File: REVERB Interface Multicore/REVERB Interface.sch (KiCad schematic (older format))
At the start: 59 parts, among them J1 RPiZeroW, J2 Iridium, J3 APRS, J4 Antenna, J5 UPDI, M1 MountingHole_Pad, M2 MountingHole_Pad, M3 MountingHole_Pad, M4 MountingHole_Pad, M5 PiMount, M6 PiMount, M7 PiMount, M8 PiMount, U1 LSM9DS1BOB, U2 MAX3232, U3 ATtiny1604-SS, U4 TXB0104D

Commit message: tie OE high
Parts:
- removed R13: 10K, Resistor_SMD:R_0805_2012Metric_Pad1.20x1.40mm_HandSolder, symbol Device:R
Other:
- moved on the sheet: J2, J3, J4, JP1, JP2, JP3, JP4

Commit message: Add decoupling
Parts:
- added C12: 22uF, Capacitor_Tantalum_SMD:CP_EIA-6032-28_Kemet-C_Pad2.25x2.35mm_HandSolder, symbol Device:CP
- added C13, C17, C18, C20, C8: 100uF, Capacitor_Tantalum_SMD:CP_EIA-7343-43_Kemet-X_Pad2.25x2.55mm_HandSolder, symbol Device:CP
- added C14, C15, C16, C19, C21, C22, C23, C9: 47uF, Capacitor_Tantalum_SMD:CP_EIA-6032-28_Kemet-C_Pad2.25x2.35mm_HandSolder, symbol Device:CP
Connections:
- wire segments 95 -> 107

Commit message: fix imu implementation on multicore branch
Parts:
- removed U1: LSM9DS1BOB, REVERB Interface:LSM9DS1BOB, symbol REVERBSym:LSM9DS1BOB
- added U1: IMU, REVERB Interface:LSM9DS1-BNO055, symbol REVERBSym:IMU
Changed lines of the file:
@@
 Wire Notes Line
 	6900 6700 6900 3650
-$Comp
-L REVERBSym:LSM9DS1BOB U1
-U 1 1 617E2B02
-P 10200 4650
-F 0 "U1" H 10678 4696 50  0000 L CNN
-F 1 "LSM9DS1BOB" H 10678 4605 50  0000 L CNN
-F 2 "REVERB Interface:LSM9DS1BOB" H 10200 4650 50  0001 C CNN
-F 3 "" H 10200 4650 50  0001 C CNN
-	1    10200 4650
-	1    0    0    -1
-$EndComp
-Text Label 9900 5050 3    50   ~ 0
+Text Label 9800 5050 3    50   ~ 0
 SW9
 Wire Wire Line
@@
 	1    0    0    -1
 $EndComp
+$Comp
+L REVERBSym:IMU U1
+U 1 1 618A2546
+P 10200 4650
+F 0 "U1" H 10678 4563 50  0000 L CNN
+F 1 "IMU" H 10678 4472 50  0000 L CNN
+F 2 "REVERB Interface:LSM9DS1-BNO055" H 10200 4650 50  0001 C CNN
+F 3 "" H 10200 4650 50  0001 C CNN
+	1    10200 4650
+	1    0    0    -1
+$EndComp

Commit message: intermediate commit
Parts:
- U1: footprint REVERB Interface:LSM9DS1-BNO055 -> REVERB Interface:BNO055
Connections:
- net EPSSCL: now also U1.5 (SCL)
- net EPSSDA: now also U1.4 (SDA)
- net GND: now also U1.3 (GND)
- net SW9: now also U1.1 (VIN)
- net IMURST: now reaches J1.32 (12(PWM0))
- net IMURST: now also U1.6 (RST)
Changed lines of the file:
@@
 Wire Notes Line
 	6900 6700 6900 3650
-Text Label 9800 5050 3    50   ~ 0
+Text Label 9950 5050 3    50   ~ 0
 SW9
 Wire Wire Line
-	10000 5050 10000 5250
+	10150 5050 10150 5250
 $Comp
 L power:GND #PWR0129
 U 1 1 617E7DA1
-P 10000 5250
-F 0 "#PWR0129" H 10000 5000 50  0001 C CNN
-F 1 "GND" H 10005 5077 50  0000 C CNN
-F 2 "" H 10000 5250 50  0001 C CNN
-F 3 "" H 10000 5250 50  0001 C CNN
-	1    10000 5250
-	1    0    0    -1
-$EndComp
-Text Label 10100 5050 3    50   ~ 0
+P 10150 5250
+F 0 "#PWR0129" H 10150 5000 50  0001 C CNN
+F 1 "GND" H 10155 5077 50  0000 C CNN
+F 2 "" H 10150 5250 50  0001 C CNN
+F 3 "" H 10150 5250 50  0001 C CNN
+	1    10150 5250
+	1    0    0    -1
+$EndComp
+Text Label 10350 5050 3    50   ~ 0
 EPSSCL
-Text Label 10200 5050 3    50   ~ 0
+Text Label 10250 5050 3    50   ~ 0
 EPSSDA
 Text Notes 9700 4200 0    50   ~ 0
@@
 F 0 "U1" H 10678 4563 50  0000 L CNN
 F 1 "IMU" H 10678 4472 50  0000 L CNN
-F 2 "REVERB Interface:LSM9DS1-BNO055" H 10200 4650 50  0001 C CNN
+F 2 "REVERB Interface:BNO055" H 10200 4650 50  0001 C CNN
 F 3 "" H 10200 4650 50  0001 C CNN
 	1    10200 4650
 	1    0    0    -1
 $EndComp
+Text Label 10450 5050 3    50   ~ 0
+IMURST
+Text Label 4600 1200 2    50   ~ 0
+IMURST
 $EndSCHEMATC

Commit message: RI line
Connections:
- net GND: now also J2.15 (Pin_15)
- net RI: now reaches J1.12 (18(PWM0))
- net RI: now also J2.8 (Pin_8)
- no-connect marks 99 -> 97
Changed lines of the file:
@@
 NoConn ~ 8800 4700
 NoConn ~ 8800 4800
-NoConn ~ 8800 4900
 NoConn ~ 8800 5000
 NoConn ~ 8800 5100
 NoConn ~ 8800 5200
-NoConn ~ 9300 4500
 NoConn ~ 9300 4800
 NoConn ~ 9300 4900
@@
 Text Label 4600 1200 2    50   ~ 0
 IMURST
+Wire Wire Line
+	9550 5000 9550 4500
+Wire Wire Line
+	9550 4500 9300 4500
+Connection ~ 9550 5000
+Text Label 8800 4900 2    50   ~ 0
+RI
+Text Label 4600 2200 2    50   ~ 0
+RI
 $EndSCHEMATC

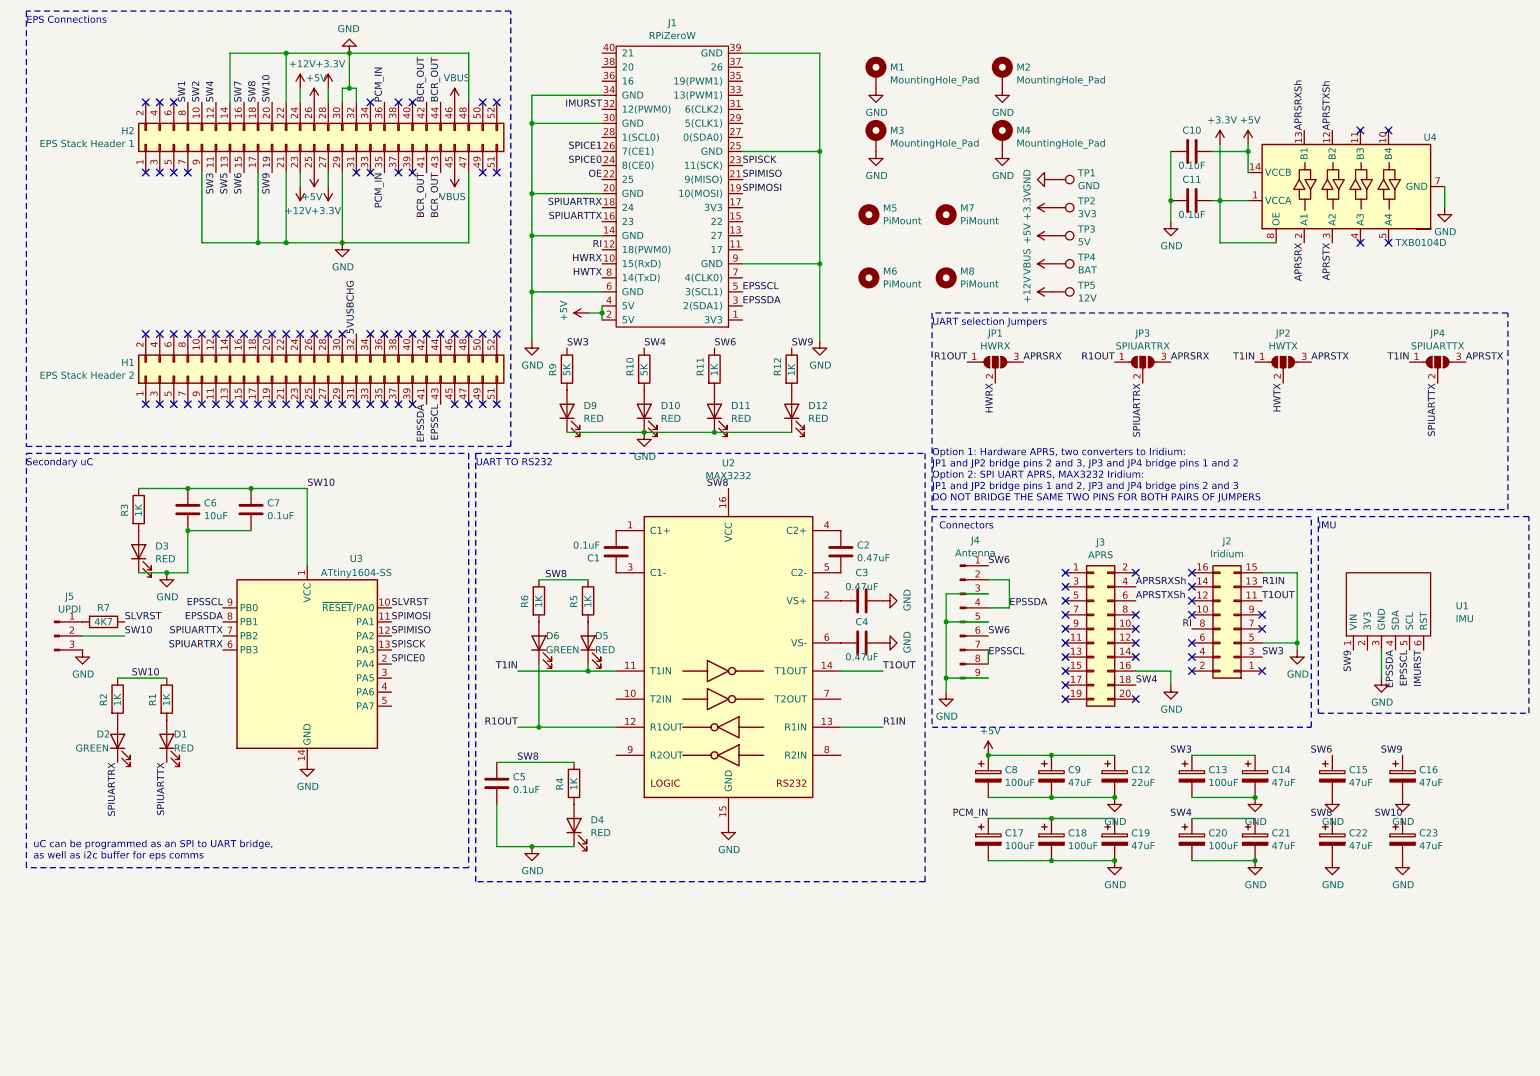
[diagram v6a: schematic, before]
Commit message: implement rtc on a pdm
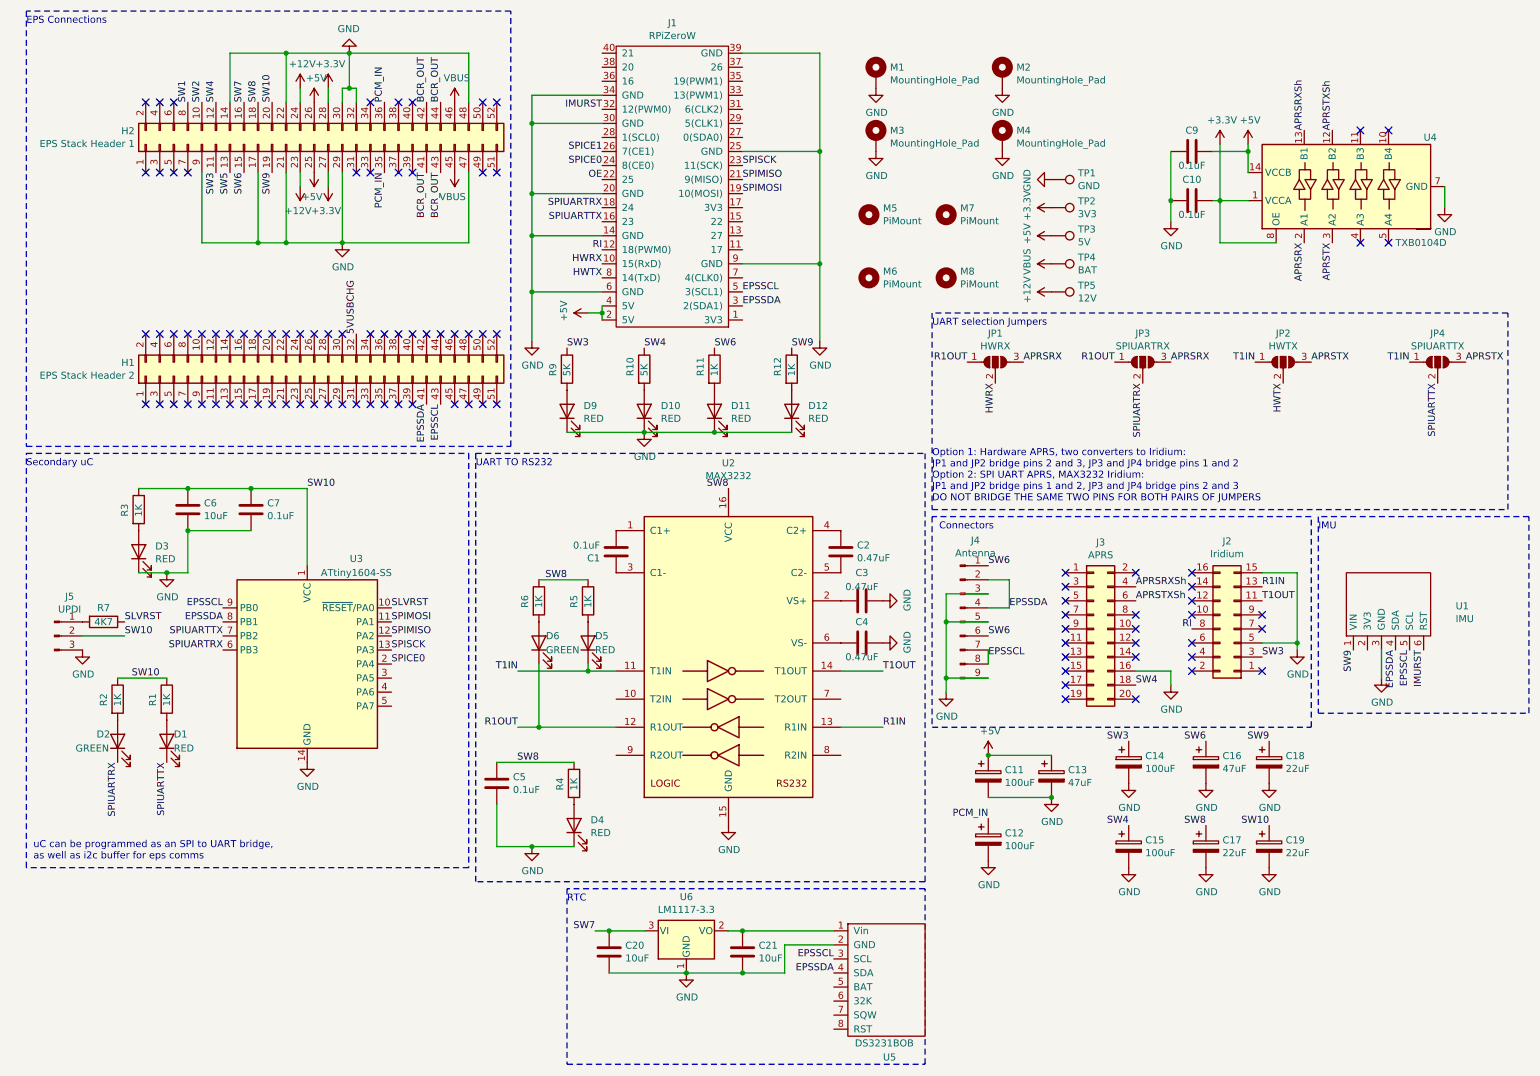
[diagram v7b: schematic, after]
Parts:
- removed C12: 22uF, Capacitor_Tantalum_SMD:CP_EIA-6032-28_Kemet-C_Pad2.25x2.35mm_HandSolder, symbol Device:CP
- removed C14, C19, C21: 47uF, Capacitor_Tantalum_SMD:CP_EIA-6032-28_Kemet-C_Pad2.25x2.35mm_HandSolder, symbol Device:CP
- removed C18: 100uF, Capacitor_Tantalum_SMD:CP_EIA-7343-43_Kemet-X_Pad2.25x2.55mm_HandSolder, symbol Device:CP
- added C20, C21: 10uF, Capacitor_SMD:C_0805_2012Metric_Pad1.18x1.45mm_HandSolder, symbol Device:C
- added U5: DS3231BOB, REVERB Interface:DS3231BOB, symbol REVERBSym:DS3231BOB
- added U6: LM1117-3.3, Package_TO_SOT_SMD:SOT-223-3_TabPin2, symbol Regulator_Linear:LM1117-3.3
- C17: renamed from C22; value 47uF -> 22uF
- C18: renamed from C16; value 47uF -> 22uF
- C19: renamed from C23; value 47uF -> 22uF
- renumbered C11 to C10, C8 to C11, C17 to C12, C9 to C13, C13 to C14, C20 to C15, C15 to C16, C10 to C9
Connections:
- net EPSSCL: now also U5.3 (SCL)
- net EPSSDA: now also U5.4 (SDA)
- net GND: now also C20.2, C21.2, U5.2 (GND), U6.1 (GND)
- net SW7: now also C20.1, U6.3 (VI)
- new net: C21.1, U5.1 (Vin), U6.2 (VO)
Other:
- note added: "RTC"
- moved on the sheet: C14, C15, C16, C17, C18, C19

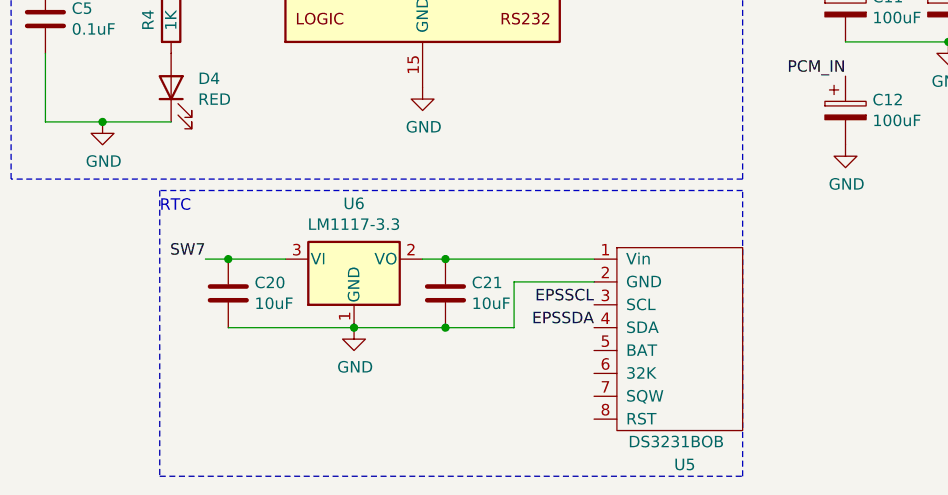
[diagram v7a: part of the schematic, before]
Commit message: embed the rtc
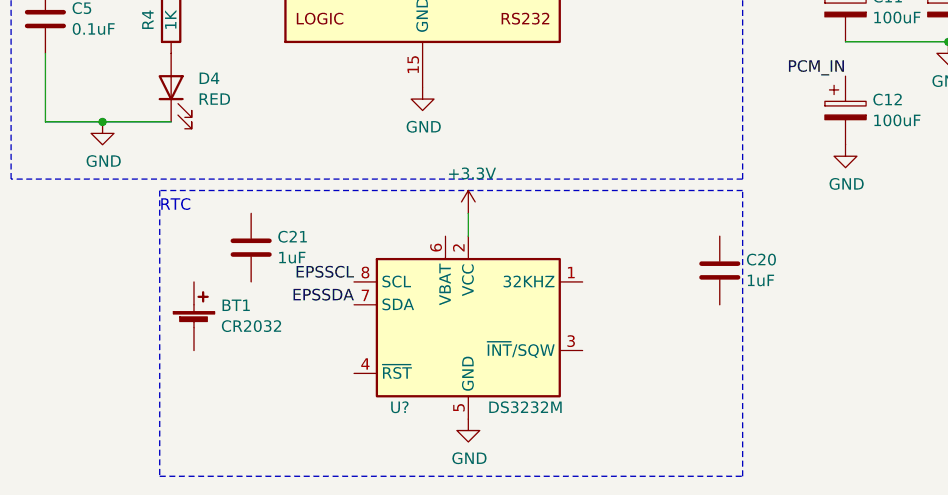
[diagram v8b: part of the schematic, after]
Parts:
- removed U5: DS3231BOB, REVERB Interface:DS3231BOB, symbol REVERBSym:DS3231BOB
- removed U6: LM1117-3.3, Package_TO_SOT_SMD:SOT-223-3_TabPin2, symbol Regulator_Linear:LM1117-3.3
- added BT1: CR2032, symbol Device:Battery_Cell
- added U?: DS3232M, Package_SO:SOIC-8_3.9x4.9mm_P1.27mm, symbol Timer_RTC:DS3232M
- C20, C21: value 10uF -> 1uF
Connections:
- net +3V3: now also U?.2 (VCC)
- net EPSSCL: now also U?.8 (SCL)
- net EPSSDA: now also U?.7 (SDA)
- net GND: now also U?.5 (GND); no longer C20.2, C21.2
- net SW7: no longer C20.1
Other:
- moved on the sheet: C20, C21
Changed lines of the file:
@@
 RI
-$Comp
-L REVERBSym:DS3231BOB U5
-U 1 1 619613C1
-P 6600 7400
-F 0 "U5" V 7150 7400 50  0000 L CNN
-F 1 "DS3231BOB" V 7050 7200 50  0000 L CNN
-F 2 "REVERB Interface:DS3231BOB" H 6600 7400 50  0001 C CNN
-F 3 "" H 6600 7400 50  0001 C CNN
-	1    6600 7400
-	0    1    1    0
-$EndComp
-$Comp
-L Regulator_Linear:LM1117-3.3 U6
-U 1 1 61963307
-P 5200 7050
-F 0 "U6" H 5200 7292 50  0000 C CNN
-F 1 "LM1117-3.3" H 5200 7201 50  0000 C CNN
-F 2 "Package_TO_SOT_SMD:SOT-223-3_TabPin2" H 5200 7050 50  0001 C CNN
-F 3 "http://www.ti.com/lit/ds/symlink/lm1117.pdf" H 5200 7050 50  0001 C CNN
-	1    5200 7050
-	1    0    0    -1
-$EndComp
-Wire Wire Line
-	5500 7050 5600 7050
-Text Label 4550 7050 2    50   ~ 0
-SW7
 $Comp
 L Device:C C21
 U 1 1 61971DD0
-P 5600 7200
-F 0 "C21" H 5715 7246 50  0000 L CNN
-F 1 "10uF" H 5715 7155 50  0000 L CNN
-F 2 "Capacitor_SMD:C_0805_2012Metric_Pad1.18x1.45mm_HandSolder" H 5638 7050 50  0001 C CNN
-F 3 "~" H 5600 7200 50  0001 C CNN
-	1    5600 7200
+P 4750 7000
+F 0 "C21" H 4865 7046 50  0000 L CNN
+F 1 "1uF" H 4865 6955 50  0000 L CNN
+F 2 "Capacitor_SMD:C_0805_2012Metric_Pad1.18x1.45mm_HandSolder" H 4788 6850 50  0001 C CNN
+F 3 "~" H 4750 7000 50  0001 C CNN
+	1    4750 7000
 	1    0    0    -1
 $EndComp
@@
 L Device:C C20
 U 1 1 619749F1
-P 4650 7200
-F 0 "C20" H 4765 7246 50  0000 L CNN
-F 1 "10uF" H 4765 7155 50  0000 L CNN
-F 2 "Capacitor_SMD:C_0805_2012Metric_Pad1.18x1.45mm_HandSolder" H 4688 7050 50  0001 C CNN
-F 3 "~" H 4650 7200 50  0001 C CNN
-	1    4650 7200
+P 6800 7100
+F 0 "C20" H 6915 7146 50  0000 L CNN
+F 1 "1uF" H 6915 7055 50  0000 L CNN
+F 2 "Capacitor_SMD:C_0805_2012Metric_Pad1.18x1.45mm_HandSolder" H 6838 6950 50  0001 C CNN
+F 3 "~" H 6800 7100 50  0001 C CNN
+	1    6800 7100
 	1    0    0    -1
 $EndComp
-Wire Wire Line
-	4550 7050 4650 7050
-Connection ~ 4650 7050
-Wire Wire Line
-	4650 7050 4900 7050
-Wire Wire Line
-	4650 7350 5200 7350
-Wire Wire Line
-	5900 7350 5900 7150
-Wire Wire Line
-	5900 7150 6250 7150
-Connection ~ 5200 7350
-Text Label 6250 7250 2    50   ~ 0
+Text Label 5200 7150 2    50   ~ 0
 EPSSCL
-Text Label 6250 7350 2    50   ~ 0
+Text Label 5200 7250 2    50   ~ 0
 EPSSDA
-Wire Wire Line
-	5200 7350 5600 7350
-Connection ~ 5600 7050
-Connection ~ 5600 7350
-Wire Wire Line
-	5600 7050 6250 7050
-Wire Wire Line
-	5600 7350 5900 7350
 $Comp
 L Device:CP C11
@@
 L power:GND #PWR?
 U 1 1 61943473
-P 5200 7350
-F 0 "#PWR?" H 5200 7100 50  0001 C CNN
-F 1 "GND" H 5205 7177 50  0000 C CNN
-F 2 "" H 5200 7350 50  0001 C CNN
-F 3 "" H 5200 7350 50  0001 C CNN
-	1    5200 7350
+P 5700 7750
+F 0 "#PWR?" H 5700 7500 50  0001 C CNN
+F 1 "GND" H 5705 7577 50  0000 C CNN
+F 2 "" H 5700 7750 50  0001 C CNN
+F 3 "" H 5700 7750 50  0001 C CNN
+	1    5700 7750
 	1    0    0    -1
 $EndComp
+$Comp
+L Timer_RTC:DS3232M U?
+U 1 1 61946450
+P 5700 7350
+F 0 "U?" H 5400 7000 50  0000 C CNN
+F 1 "DS3232M" H 5950 7000 50  0000 C CNN
+F 2 "Package_SO:SOIC-8_3.9x4.9mm_P1.27mm" H 5750 6850 50  0001 C CNN
+F 3 "http://datasheets.maximintegrated.com/en/ds/DS3232M.pdf" H 5970 7500 50  0001 C CNN
+	1    5700 7350
+	1    0    0    -1
+$EndComp
+$Comp
+L power:+3.3V #PWR?
+U 1 1 61947E10
+P 5700 6850
+F 0 "#PWR?" H 5700 6700 50  0001 C CNN
+F 1 "+3.3V" H 5715 7023 50  0000 C CNN
+F 2 "" H 5700 6850 50  0001 C CNN
+F 3 "" H 5700 6850 50  0001 C CNN
+	1    5700 6850
+	1    0    0    -1
+$EndComp
+Wire Wire Line
+	5700 6850 5700 6950
+$Comp
+L Device:Battery_Cell BT1
+U 1 1 6194D163
+P 4500 7350
+F 0 "BT1" H 4618 7446 50  0000 L CNN
+F 1 "CR2032" H 4618 7355 50  0000 L CNN
+F 2 "" V 4500 7410 50  0001 C CNN
+F 3 "~" V 4500 7410 50  0001 C CNN
+	1    4500 7350
+	1    0    0    -1
+$EndComp
